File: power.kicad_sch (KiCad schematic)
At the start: 21 parts, among them U101 HT7533-1, U102 TLV62569DBV, U103 MCP6001T-E/OT

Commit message: Reannotate based on sheet page number
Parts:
- renumbered C109 to C201, C101 to C202, C102 to C203, C103 to C204, C104 to C205, C108 to C206, C105 to C207, C106 to C208, C107 to C209, D101 to D201, L101 to L201, L102 to L202, R101 to R201, R105 to R202, R106 to R203, R102 to R204, R104 to R205, R103 to R206, U101 to U201, U103 to U202, U102 to U203

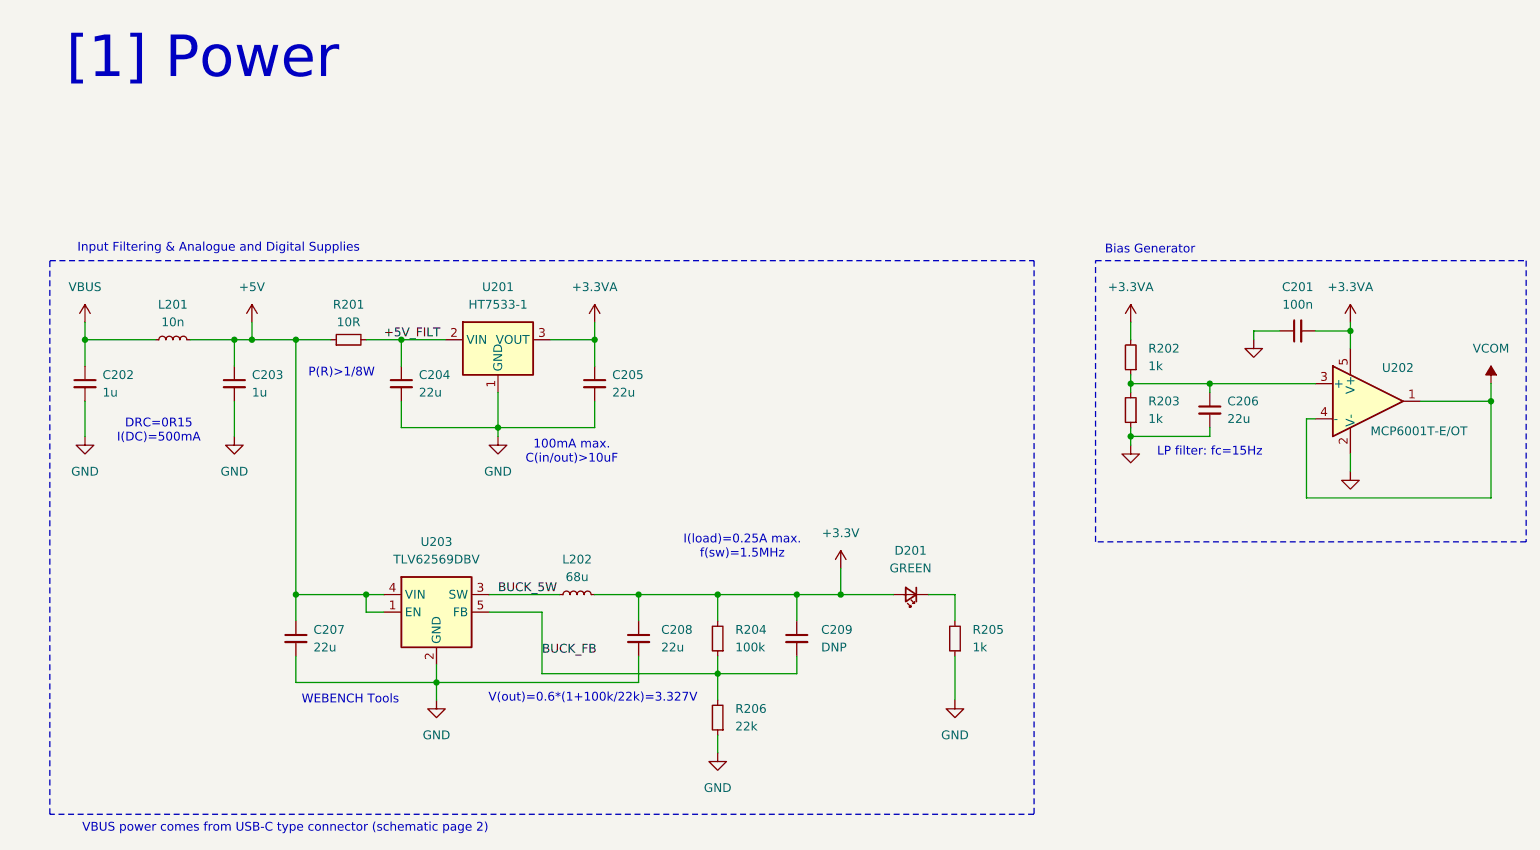
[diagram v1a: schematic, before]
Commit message: Lesson 6: MCU and USB module
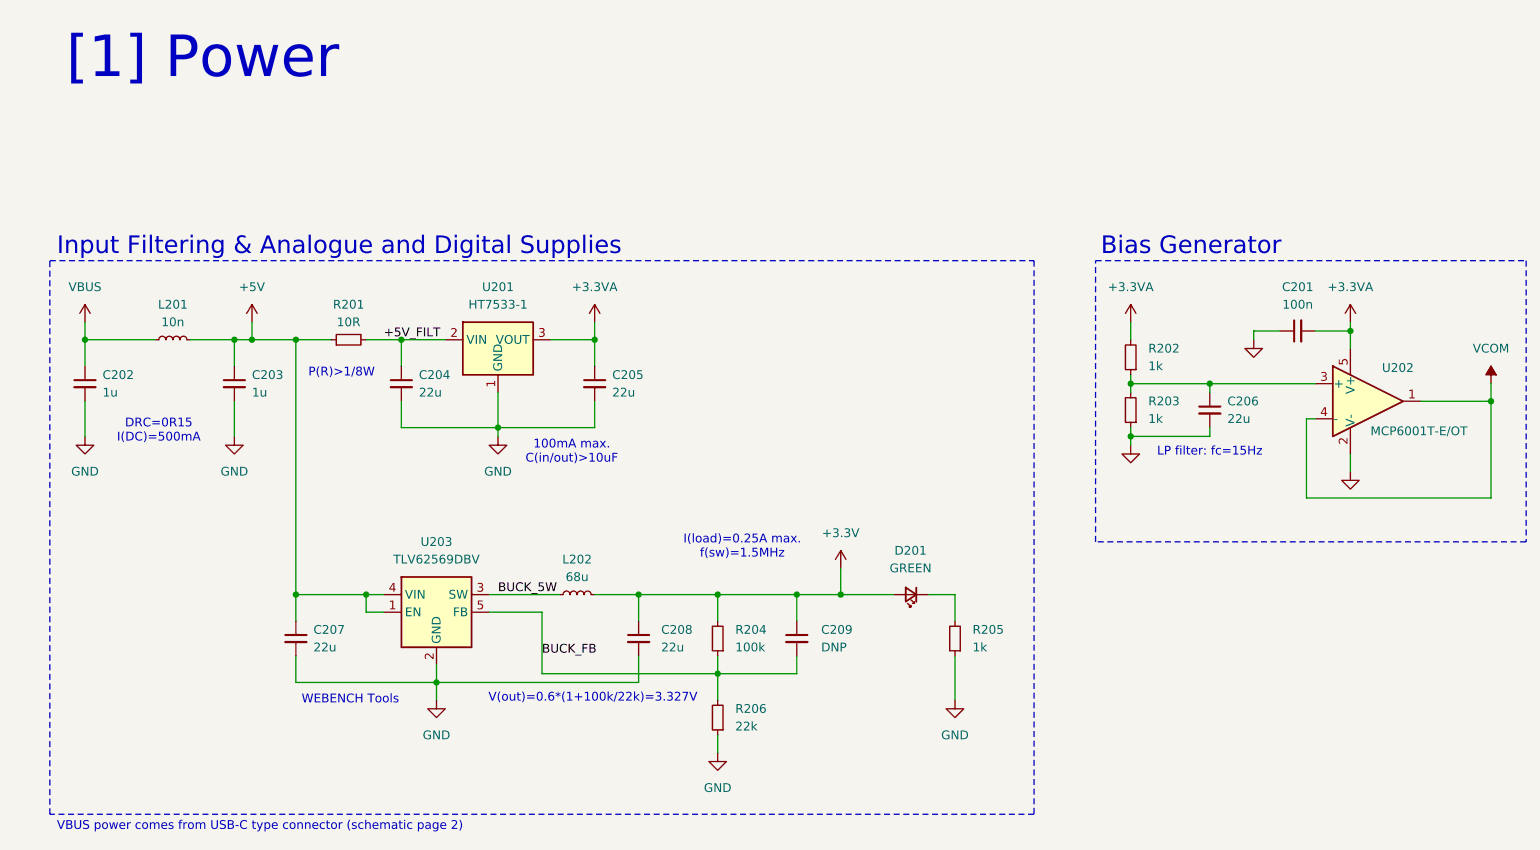
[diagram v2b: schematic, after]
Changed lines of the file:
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@@
 	(text "Bias Generator"
 		(exclude_from_sim no)
-		(at 188.214 50.546 0)
+		(at 181.102 50.038 0)
 		(effects
 			(font
-				(size 1.27 1.27)
+				(size 2.54 2.54)
 			)
+			(justify left)
 		)
 	)
@@
 	(text "VBUS power comes from USB-C type connector (schematic page 2)"
 		(exclude_from_sim no)
-		(at 63.246 134.112 0)
+		(at 30.226 133.858 0)
 		(effects
 			(font
 				(size 1.27 1.27)
 			)
+			(justify left)
 		)
 	)
@@
 	(text "Input Filtering & Analogue and Digital Supplies"
 		(exclude_from_sim no)
-		(at 53.594 50.292 0)
+		(at 30.226 50.038 0)
 		(effects
 			(font
-				(size 1.27 1.27)
+				(size 2.54 2.54)
 			)
+			(justify left)
 		)
 	)

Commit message: Lesson 8: Assigned most footprints. Added missing ones
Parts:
- C201, C202, C203, C209: footprint (none) -> Capacitor_SMD:C_0402_1005Metric
- C204, C205, C206, C207, C208: footprint (none) -> Capacitor_SMD:C_0603_1608Metric
- D201: footprint (none) -> LED_SMD:LED_0402_1005Metric
- L201, L202: footprint (none) -> Inductor_SMD:L_0603_1608Metric
- R201, R204, R206: footprint (none) -> Resistor_SMD:R_0603_1608Metric
- R202, R203, R205: footprint (none) -> Resistor_SMD:R_0402_1005Metric
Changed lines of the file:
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@@
 			)
 		)
-		(property "Footprint" ""
+		(property "Footprint" "Inductor_SMD:L_0603_1608Metric"
 			(at 46.99 63.5 0)
 			(effects
@@
 			)
 		)
-		(property "Footprint" ""
+		(property "Footprint" "LED_SMD:LED_0402_1005Metric"
 			(at 153.67 100.33 90)
 			(effects
@@
 			)
 		)
-		(property "Footprint" ""
+		(property "Footprint" "Resistor_SMD:R_0603_1608Metric"
 			(at 125.73 118.11 0)
 			(effects
@@
 			)
 		)
-		(property "Footprint" ""
+		(property "Footprint" "Capacitor_SMD:C_0603_1608Metric"
 			(at 114.3 106.68 0)
 			(effects
@@
 			)
 		)
-		(property "Footprint" ""
+		(property "Footprint" "Capacitor_SMD:C_0402_1005Metric"
 			(at 34.29 69.85 0)
 			(effects
@@
 			)
 		)
-		(property "Footprint" ""
+		(property "Footprint" "Resistor_SMD:R_0402_1005Metric"
 			(at 160.02 106.68 0)
 			(effects
@@
 			)
 		)
-		(property "Footprint" ""
+		(property "Footprint" "Capacitor_SMD:C_0402_1005Metric"
 			(at 209.55 62.23 0)
 			(effects
@@
 			)
 		)
-		(property "Footprint" ""
+		(property "Footprint" "Capacitor_SMD:C_0603_1608Metric"
 			(at 196.85 73.66 0)
 			(effects
@@
 			)
 		)
-		(property "Footprint" ""
+		(property "Footprint" "Capacitor_SMD:C_0603_1608Metric"
 			(at 107.95 69.85 0)
 			(effects
@@
 			)
 		)
-		(property "Footprint" ""
+		(property "Footprint" "Inductor_SMD:L_0603_1608Metric"
 			(at 105.41 100.33 0)
 			(effects
@@
 			)
 		)
-		(property "Footprint" ""
+		(property "Footprint" "Resistor_SMD:R_0603_1608Metric"
 			(at 72.39 63.5 0)
 			(effects
@@
 			)
 		)
-		(property "Footprint" ""
+		(property "Footprint" "Resistor_SMD:R_0402_1005Metric"
 			(at 185.42 66.04 0)
 			(effects
@@
 			)
 		)
-		(property "Footprint" ""
+		(property "Footprint" "Resistor_SMD:R_0603_1608Metric"
 			(at 125.73 106.68 0)
 			(effects
@@
 			)
 		)
-		(property "Footprint" ""
+		(property "Footprint" "Capacitor_SMD:C_0603_1608Metric"
 			(at 80.01 69.85 0)
 			(effects
@@
 			)
 		)
-		(property "Footprint" ""
+		(property "Footprint" "Capacitor_SMD:C_0402_1005Metric"
 			(at 137.16 106.68 0)
 			(effects
@@
 			)
 		)
-		(property "Footprint" ""
+		(property "Footprint" "Resistor_SMD:R_0402_1005Metric"
 			(at 185.42 73.66 0)
 			(effects
@@
 			)
 		)
-		(property "Footprint" ""
+		(property "Footprint" "Capacitor_SMD:C_0402_1005Metric"
 			(at 55.88 69.85 0)
 			(effects
@@
 			)
 		)
-		(property "Footprint" ""
+		(property "Footprint" "Capacitor_SMD:C_0603_1608Metric"
 			(at 64.77 106.68 0)
 			(effects

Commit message: Lesson 11: Adjusted capacitor footprints and set up PCB defaults
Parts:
- C202, C203: footprint Capacitor_SMD:C_0402_1005Metric -> Capacitor_SMD:C_0603_1608Metric
- C204, C205, C206, C207, C208: footprint Capacitor_SMD:C_0603_1608Metric -> Capacitor_SMD:C_0805_2012Metric
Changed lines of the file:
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@@
 			)
 		)
-		(property "Footprint" "Capacitor_SMD:C_0603_1608Metric"
+		(property "Footprint" "Capacitor_SMD:C_0805_2012Metric"
 			(at 114.3 106.68 0)
 			(effects
@@
 			)
 		)
-		(property "Footprint" "Capacitor_SMD:C_0402_1005Metric"
+		(property "Footprint" "Capacitor_SMD:C_0603_1608Metric"
 			(at 34.29 69.85 0)
 			(effects
@@
 			)
 		)
-		(property "Footprint" "Capacitor_SMD:C_0603_1608Metric"
+		(property "Footprint" "Capacitor_SMD:C_0805_2012Metric"
 			(at 196.85 73.66 0)
 			(effects
@@
 			)
 		)
-		(property "Footprint" "Capacitor_SMD:C_0603_1608Metric"
+		(property "Footprint" "Capacitor_SMD:C_0805_2012Metric"
 			(at 107.95 69.85 0)
 			(effects
@@
 			)
 		)
-		(property "Footprint" "Capacitor_SMD:C_0603_1608Metric"
+		(property "Footprint" "Capacitor_SMD:C_0805_2012Metric"
 			(at 80.01 69.85 0)
 			(effects
@@
 			)
 		)
-		(property "Footprint" "Capacitor_SMD:C_0402_1005Metric"
+		(property "Footprint" "Capacitor_SMD:C_0603_1608Metric"
 			(at 55.88 69.85 0)
 			(effects
@@
 			)
 		)
-		(property "Footprint" "Capacitor_SMD:C_0603_1608Metric"
+		(property "Footprint" "Capacitor_SMD:C_0805_2012Metric"
 			(at 64.77 106.68 0)
 			(effects

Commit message: Lesson 12: Rest of placement, some rearrangements. Added models
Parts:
- L201: footprint Inductor_SMD:L_0603_1608Metric -> Inductor_SMD:L_0402_1005Metric
- L202: footprint Inductor_SMD:L_0603_1608Metric -> Inductor_SMD:L_Coilcraft_XxL4020; MPN (none) -> C3151182
- R201: footprint Resistor_SMD:R_0603_1608Metric -> Resistor_SMD:R_0805_2012Metric
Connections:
- net VREF: now reaches C206.1, R202.1, R203.2, U202.3 (+)
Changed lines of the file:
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@@
 		)
 	)
-	(label "BUCK_FB"
-		(at 100.33 109.22 0)
+	(label "VREF"
+		(at 204.47 69.85 0)
 		(fields_autoplaced yes)
 		(effects
@@
 		)
 	)
-	(label "+5V_FILT"
-		(at 77.47 63.5 0)
+	(label "BUCK_FB"
+		(at 100.33 109.22 0)
 		(fields_autoplaced yes)
 		(effects
@@
 		)
 	)
-	(label "BUCK_5W"
-		(at 93.98 100.33 0)
+	(label "+5V_FILT"
+		(at 77.47 63.5 0)
 		(fields_autoplaced yes)
 		(effects
@@
 		)
 	)
+	(label "BUCK_5W"
+		(at 93.98 100.33 0)
+		(fields_autoplaced yes)
+		(effects
+			(font
+				(size 1.27 1.27)
+			)
+			(justify left bottom)
+		)
+	)
 	(symbol
 		(lib_id "power:GND")
@@
 			)
 		)
-		(property "Footprint" "Inductor_SMD:L_0603_1608Metric"
+		(property "Footprint" "Inductor_SMD:L_0402_1005Metric"
 			(at 46.99 63.5 0)
 			(effects
@@
 			)
 		)
-		(property "Footprint" "Inductor_SMD:L_0603_1608Metric"
+		(property "Footprint" "Inductor_SMD:L_Coilcraft_XxL4020"
 			(at 105.41 100.33 0)
 			(effects
@@
 			)
 		)
+		(property "MPN" "C3151182"
+			(at 105.41 100.33 90)
+			(effects
+				(font
+					(size 1.27 1.27)
+				)
+				(hide yes)
+			)
+		)
 		(pin "1"
 		)
@@
 			)
 		)
-		(property "Footprint" "Resistor_SMD:R_0603_1608Metric"
+		(property "Footprint" "Resistor_SMD:R_0805_2012Metric"
 			(at 72.39 63.5 0)
 			(effects

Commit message: Lesson 13: Routing
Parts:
- R204, R206: footprint Resistor_SMD:R_0603_1608Metric -> Resistor_SMD:R_0402_1005Metric
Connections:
- net BUCK_5W renamed BUCK_SW
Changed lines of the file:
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@@
 		)
 	)
-	(label "BUCK_5W"
+	(label "BUCK_SW"
 		(at 93.98 100.33 0)
 		(fields_autoplaced yes)
@@
 			)
 		)
-		(property "Footprint" "Resistor_SMD:R_0603_1608Metric"
+		(property "Footprint" "Resistor_SMD:R_0402_1005Metric"
 			(at 125.73 118.11 0)
 			(effects
@@
 			)
 		)
-		(property "Footprint" "Resistor_SMD:R_0603_1608Metric"
+		(property "Footprint" "Resistor_SMD:R_0402_1005Metric"
 			(at 125.73 106.68 0)
 			(effects

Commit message: Assembly files
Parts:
- C201: MPN (none) -> C1525
- C202, C203: MPN (none) -> C15849
- C204, C205, C206, C207, C208: MPN (none) -> C45783
- C209: now not fitted
- D201: value GREEN -> RED; footprint LED_SMD:LED_0402_1005Metric -> LED_SMD:LED_0603_1608Metric; MPN (none) -> C2286
- L201: MPN (none) -> C404632
- R201: MPN (none) -> C17415
- R202, R203, R205: MPN (none) -> C11702
- R204: MPN (none) -> 0402
- R206: MPN (none) -> C25768
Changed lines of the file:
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@@
+			)
+		)
+		(property "MPN" "C404632"
+			(at 46.99 63.5 0)
+			(effects
+				(font
+					(size 1.27 1.27)
+				)
+				(hide yes)
 			)
 		)
@@
 			)
 		)
-		(property "Value" "GREEN"
+		(property "Value" "RED"
 			(at 153.6065 96.52 0)
 			(effects
@@
 			)
 		)
-		(property "Footprint" "LED_SMD:LED_0402_1005Metric"
+		(property "Footprint" "LED_SMD:LED_0603_1608Metric"
 			(at 153.67 100.33 90)
 			(effects
@@
 			)
 		)
+		(property "MPN" "C2286"
+			(at 153.67 100.33 0)
+			(effects
+				(font
+					(size 1.27 1.27)
+				)
+				(hide yes)
+			)
+		)
 		(pin "2"
 		)
@@
 			)
 		)
+		(property "MPN" "C25768"
+			(at 125.73 118.11 0)
+			(effects
+				(font
+					(size 1.27 1.27)
+				)
+				(hide yes)
+			)
+		)
 		(pin "2"
 		)
@@
 			)
 		)
+		(property "MPN" "C45783"
+			(at 114.3 106.68 0)
+			(effects
+				(font
+					(size 1.27 1.27)
+				)
+				(hide yes)
+			)
+		)
 		(pin "2"
 		)
@@
 			)
 		)
+		(property "MPN" "C15849"
+			(at 34.29 69.85 0)
+			(effects
+				(font
+					(size 1.27 1.27)
+				)
+				(hide yes)
+			)
+		)
 		(pin "2"
 		)
@@
 			)
 		)
+		(property "MPN" "C11702"
+			(at 160.02 106.68 0)
+			(effects
+				(font
+					(size 1.27 1.27)
+				)
+				(hide yes)
+			)
+		)
 		(pin "2"
 		)
@@
 			)
 		)
+		(property "MPN" "C1525"
+			(at 209.55 62.23 0)
+			(effects
+				(font
+					(size 1.27 1.27)
+				)
+				(hide yes)
+			)
+		)
 		(pin "2"
 		)
@@
 			)
 		)
+		(property "MPN" "C45783"
+			(at 196.85 73.66 0)
+			(effects
+				(font
+					(size 1.27 1.27)
+				)
+				(hide yes)
+			)
+		)
 		(pin "2"
 		)
@@
 			)
 		)
+		(property "MPN" "C45783"
+			(at 107.95 69.85 0)
+			(effects
+				(font
+					(size 1.27 1.27)
+				)
+				(hide yes)
+			)
+		)
 		(pin "2"
 		)
@@
 			)
 		)
+		(property "MPN" "C17415"
+			(at 72.39 63.5 0)
+			(effects
+				(font
+					(size 1.27 1.27)
+				)
+				(hide yes)
+			)
+		)
 		(pin "2"
 		)
@@
 			)
 		)
+		(property "MPN" "C11702"
+			(at 185.42 66.04 0)
+			(effects
+				(font
+					(size 1.27 1.27)
+				)
+				(hide yes)
+			)
+		)
 		(pin "2"
 		)
@@
 			)
 		)
+		(property "MPN" "0402"
+			(at 125.73 106.68 0)
+			(effects
+				(font
+					(size 1.27 1.27)
+				)
+				(hide yes)
+			)
+		)
 		(pin "2"
 		)
@@
 			)
 		)
+		(property "MPN" "C45783"
+			(at 80.01 69.85 0)
+			(effects
+				(font
+					(size 1.27 1.27)
+				)
+				(hide yes)
+			)
+		)
 		(pin "2"
 		)
@@
 		(in_bom yes)
 		(on_board yes)
-		(dnp no)
+		(dnp yes)
 		(fields_autoplaced yes)
 		(property "Reference" "C209"
@@
 			)
 		)
+		(property "MPN" "C11702"
+			(at 185.42 73.66 0)
+			(effects
+				(font
+					(size 1.27 1.27)
+				)
+				(hide yes)
+			)
+		)
 		(pin "2"
 		)
@@
 			)
 		)
+		(property "MPN" "C15849"
+			(at 55.88 69.85 0)
+			(effects
+				(font
+					(size 1.27 1.27)
+				)
+				(hide yes)
+			)
+		)
 		(pin "2"
 		)
@@
 			(at 64.77 106.68 0)
 			(effects
+				(font
+					(size 1.27 1.27)
+				)
+				(hide yes)
+			)
+		)
+		(property "MPN" "C45783"
+			(at 64.77 106.68 0)
+			(effects
